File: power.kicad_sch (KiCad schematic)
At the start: 89 parts, among them Q1 PJE138K, Q2 PJE138K, Q3 SSM3J332R, Q4 PJE138K, Q5 SSM3J332R, Q6 PJE138K, Q7 SSM3J332R, U1 TLV70018_SC70, U4 TPS65150_HTSSOP, U5 MPQ7235GQBE, U6 TLV76701_WSON

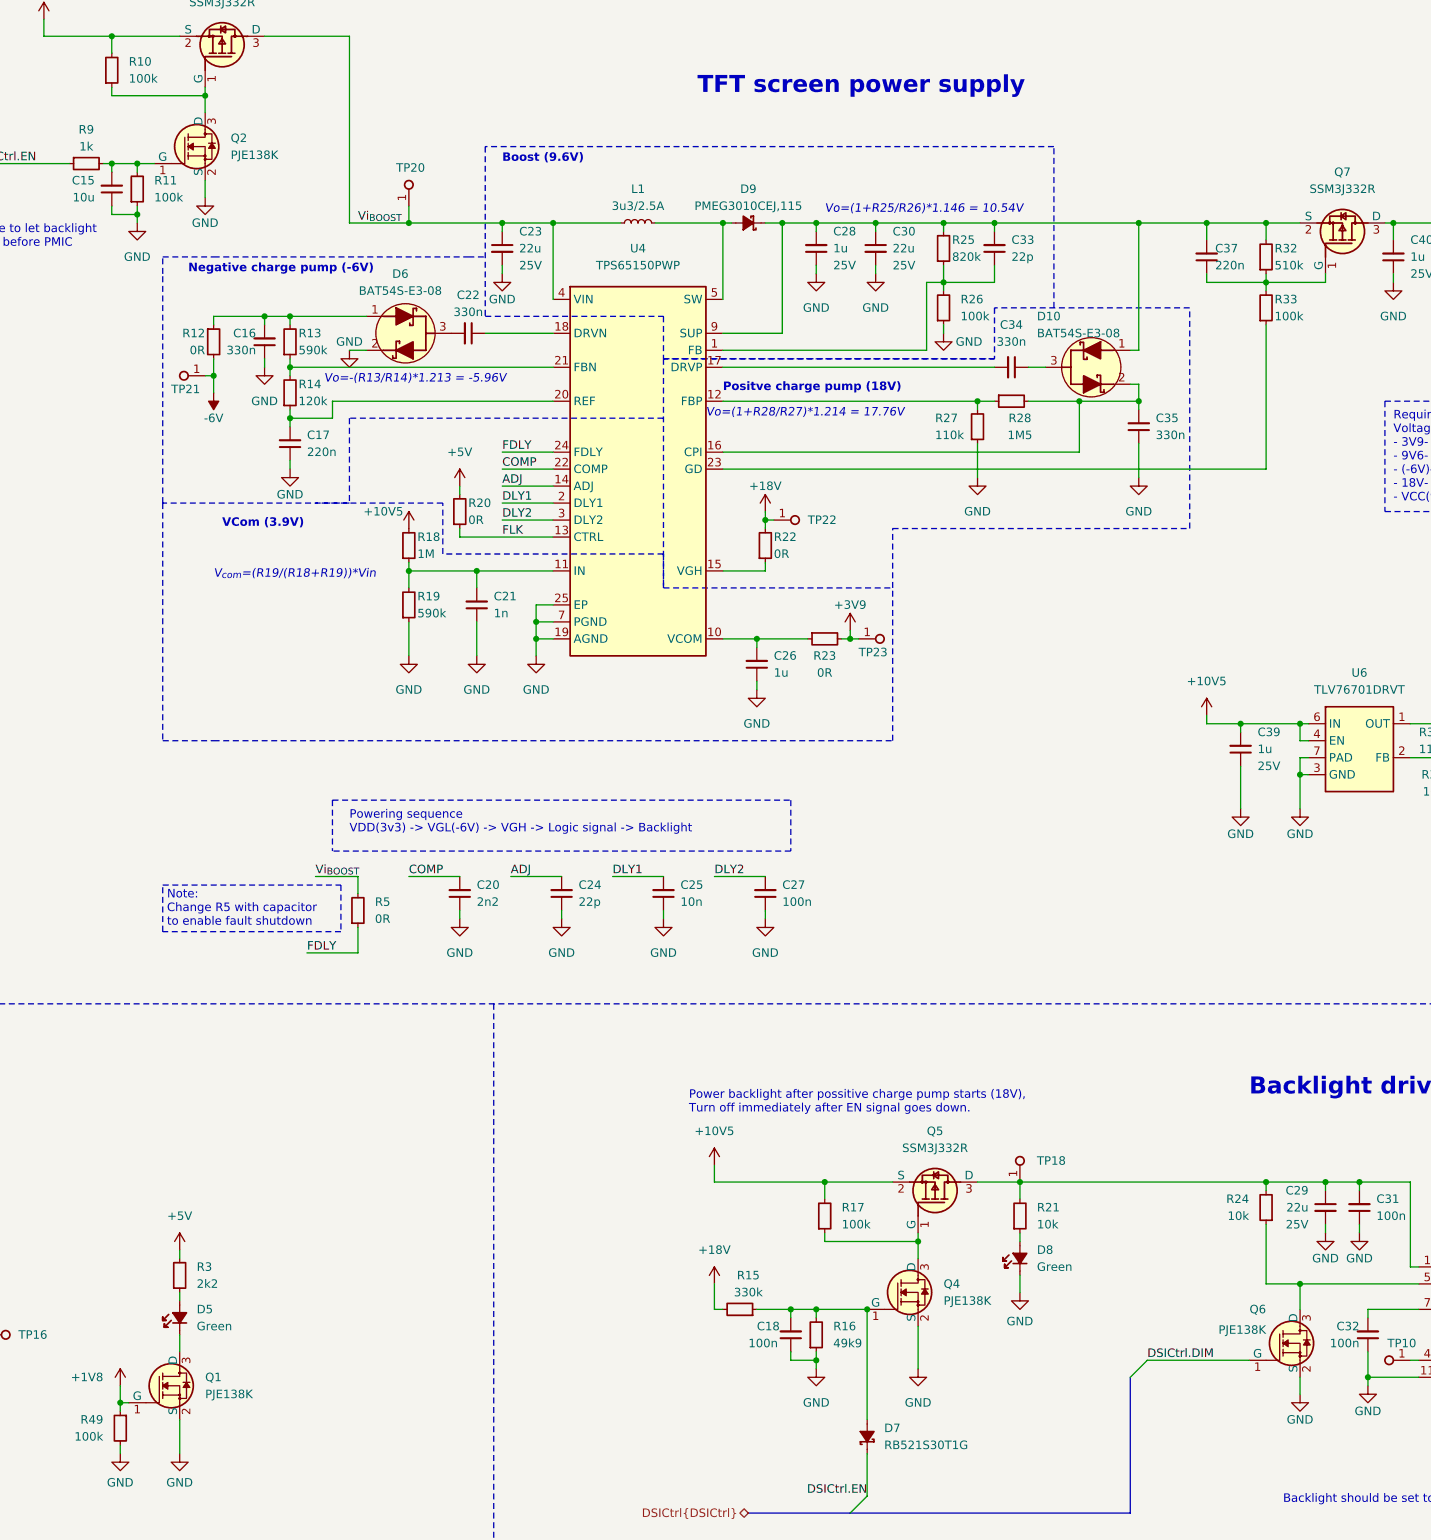
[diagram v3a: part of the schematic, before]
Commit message: [#61475] Update symbols from library & resolve ERC issues
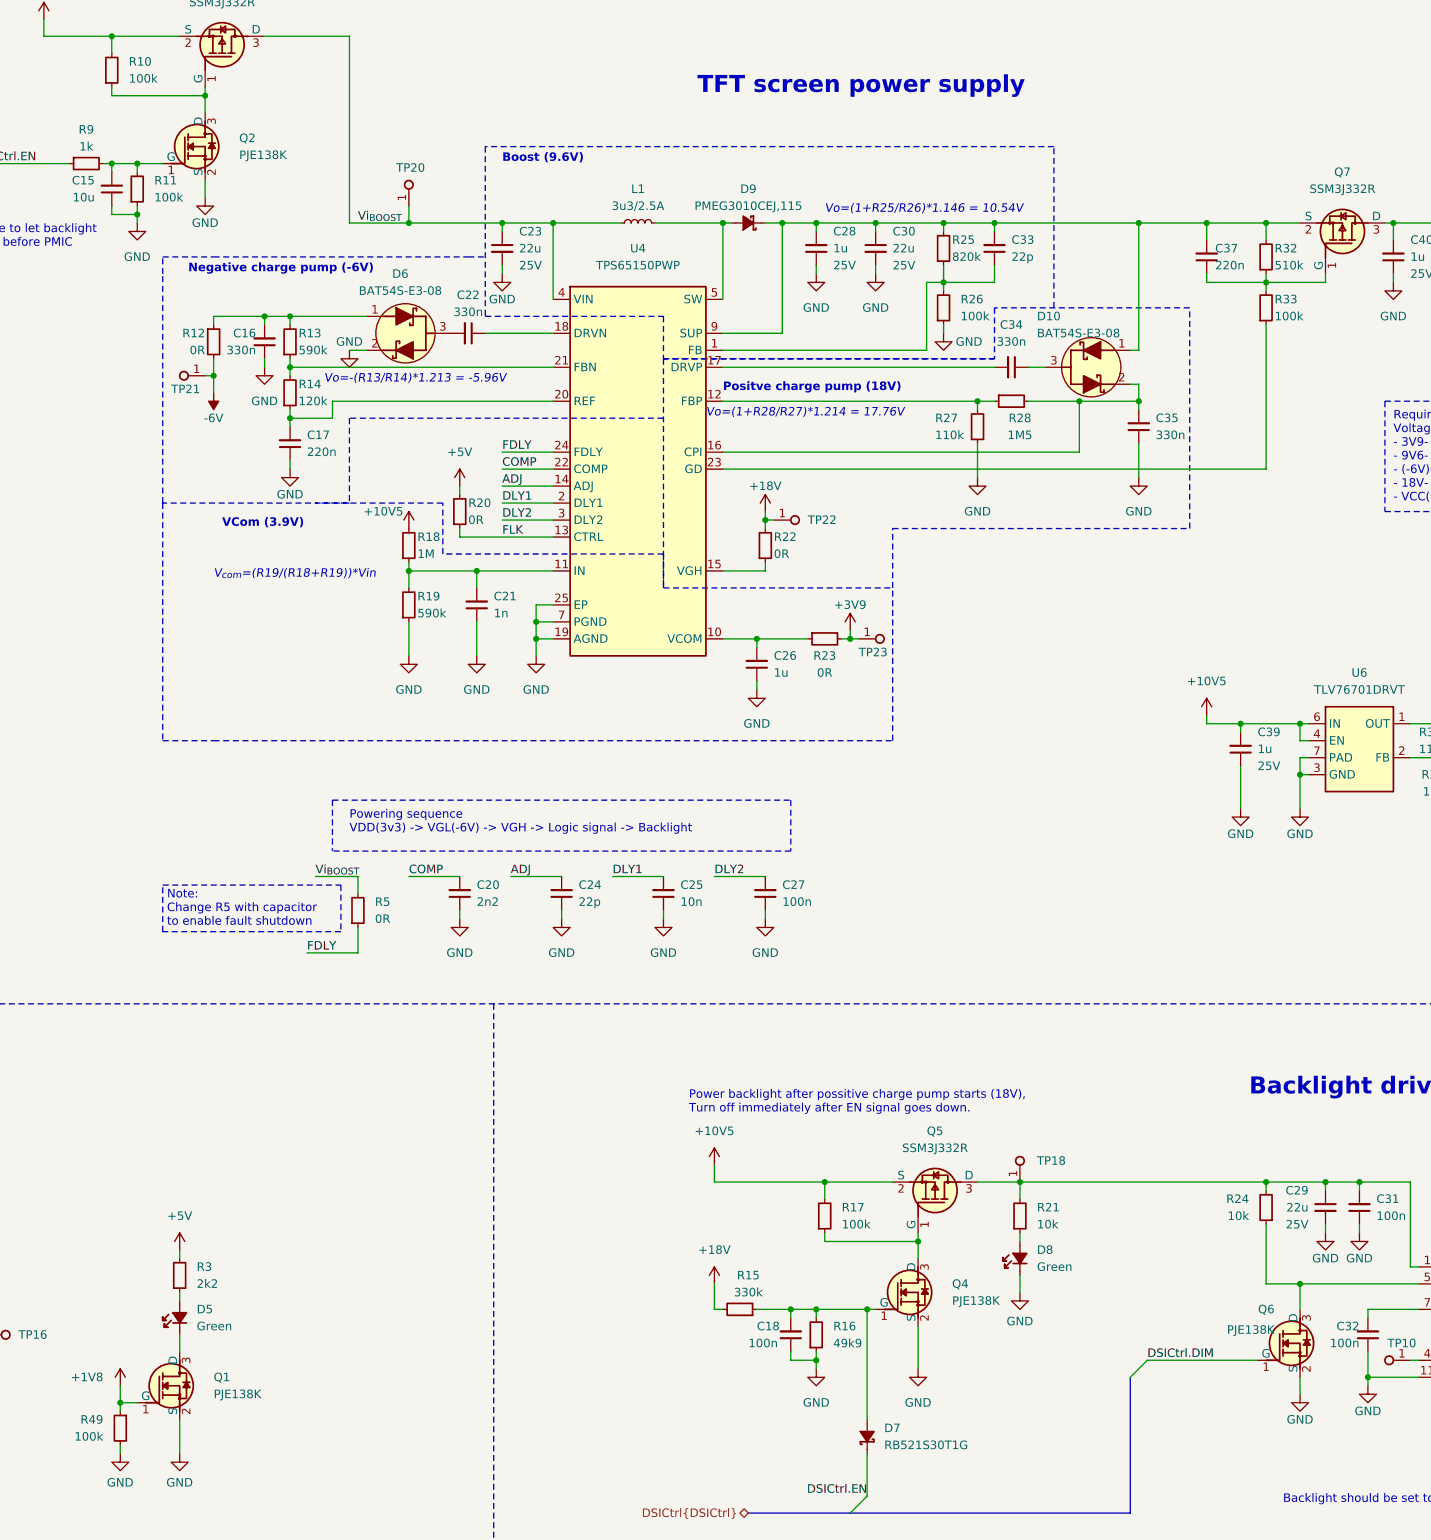
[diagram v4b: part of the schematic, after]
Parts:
- C15, C16, C17, C18, C2, C20, C21, C22, C23, C24, C25, C26, C27, C28, C29, C3, C30, C31, C32, C33, C34, C35, C36, C37, C38, C39, C40, C41, D11, D5, D7, D8, D9, L1, L2, R10, R11, R12, R13, R14, R15, R16, R17, R18, R19, R20, R21, R22, R23, R24, R25, R26, R27, R28, R29, R3, R30, R31, R32, R33, R34, R35, R36, R37, R38, R49, R5, R9, TP10, TP11, TP16, TP18, TP20, TP21, TP22, TP23: Public (none) -> False
